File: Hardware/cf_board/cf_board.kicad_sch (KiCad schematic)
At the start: 14 parts, among them J1 Conn_01x40, J2 Conn_02x25_Top_Bottom, U1 74HC00, U2 74HC00

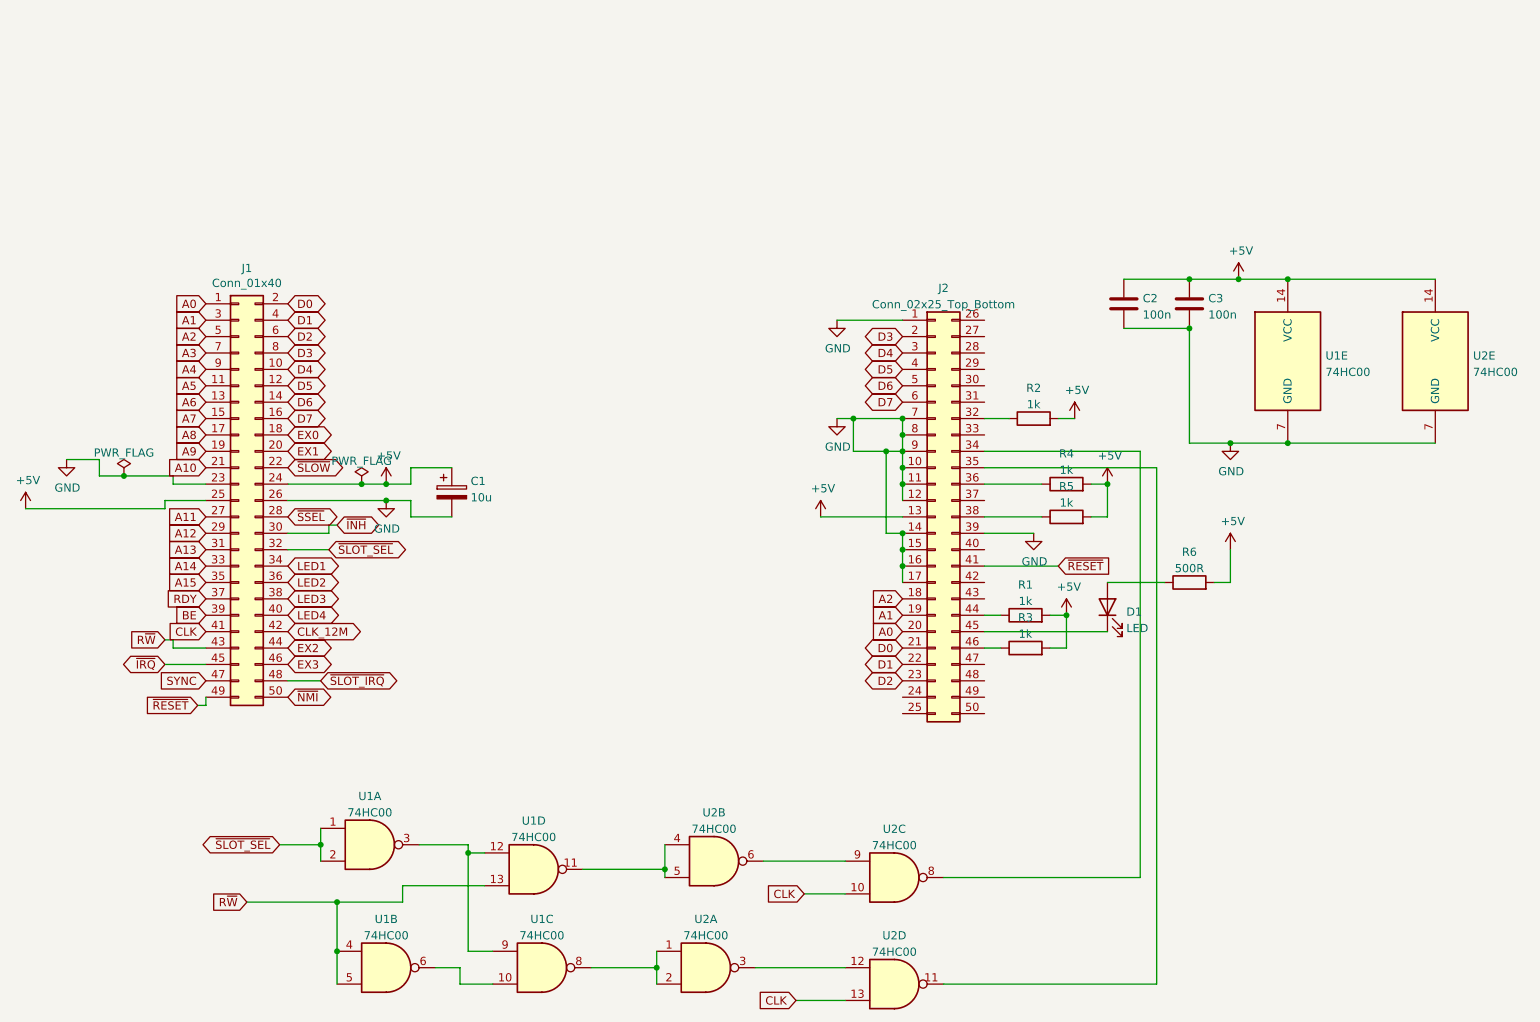
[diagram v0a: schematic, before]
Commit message: update with lcsc CF card socket
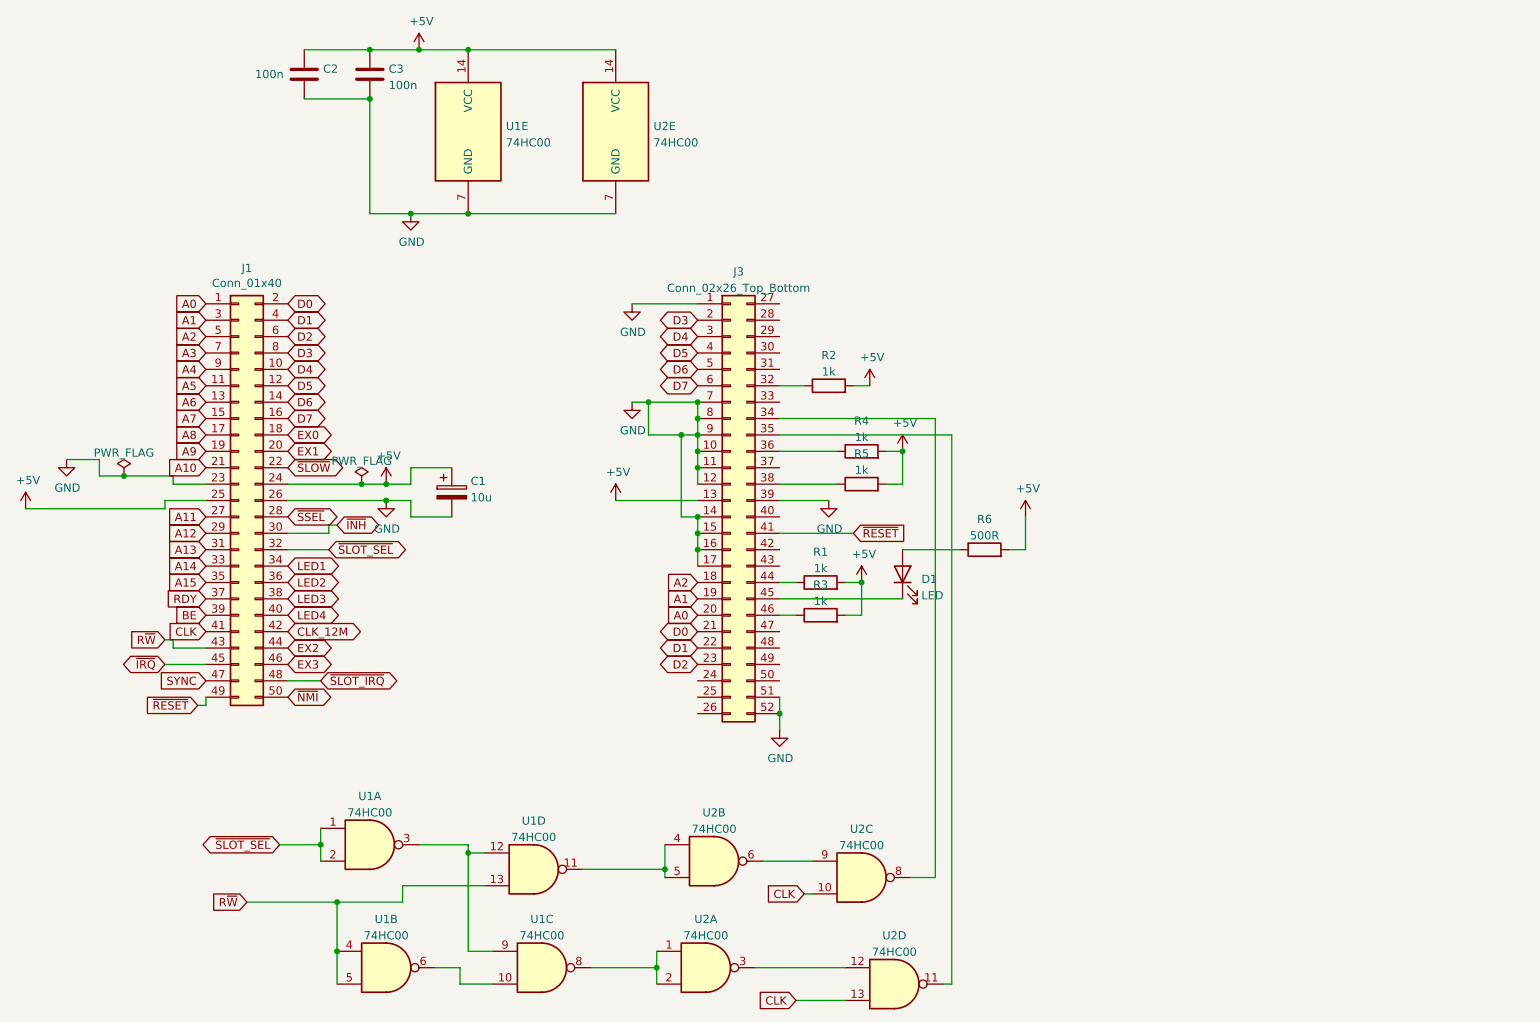
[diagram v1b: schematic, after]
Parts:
- removed J2: Conn_02x25_Top_Bottom, Connector_Card:CF-Card_3M_N7E50-A516xx-30, symbol Connector_Generic:Conn_02x25_Top_Bottom
- added J3: Conn_02x26_Top_Bottom, Custom_Footprints:SD-SMD_CFH-L3C1LBL01MN0, symbol Connector_Generic:Conn_02x26_Top_Bottom
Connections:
- net +5V: now also J3.13 (Pin_13)
- net A0: now also J3.20 (Pin_20)
- net A1: now also J3.19 (Pin_19)
- net A2: now also J3.18 (Pin_18)
- net D0: now also J3.21 (Pin_21)
- net D1: now also J3.22 (Pin_22)
- net D2: now also J3.23 (Pin_23)
- net D3: now also J3.2 (Pin_2)
- net D4: now also J3.3 (Pin_3)
- net D5: now also J3.4 (Pin_4)
- net D6: now also J3.5 (Pin_5)
- net D7: now also J3.6 (Pin_6)
- net GND: now also J3.1 (Pin_1), J3.10 (Pin_10), J3.11 (Pin_11), J3.12 (Pin_12), J3.14 (Pin_14), J3.15 (Pin_15), J3.16 (Pin_16), J3.17 (Pin_17), J3.39 (Pin_39), J3.51 (Pin_51), J3.52 (Pin_52), J3.7 (Pin_7), J3.8 (Pin_8), J3.9 (Pin_9)
- net ~{RESET}: now also J3.41 (Pin_41)
- net at R2.1: now also J3.32 (Pin_32)
- net at R3.1: now also J3.46 (Pin_46)
- net at U2.8: now also J3.34 (Pin_34)
- net at U2.11: now also J3.35 (Pin_35)
- net at D1.1 (K): now also J3.45 (Pin_45)
- net at R5.1: now also J3.38 (Pin_38)
- net at R4.1: now also J3.36 (Pin_36)
- net at R1.1: now also J3.44 (Pin_44)
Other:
- moved on the sheet: C2, C3, D1, R1, R2, R3, R4, R5, R6, U1E, U2C, U2E

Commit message: CF card works as block storage for forth
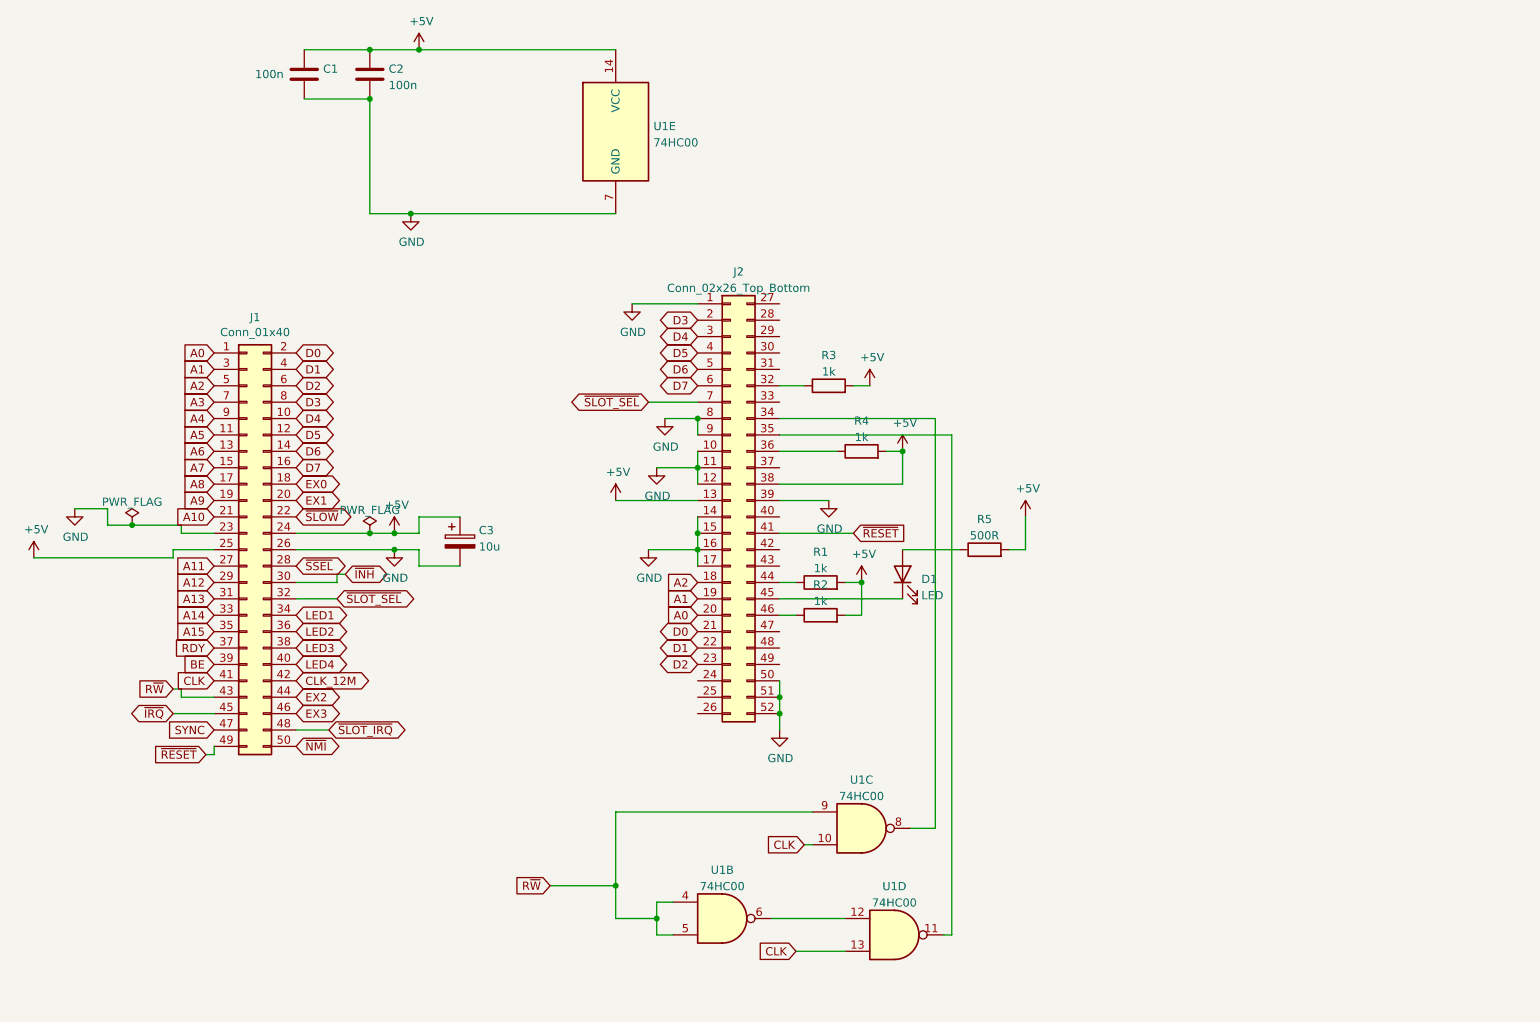
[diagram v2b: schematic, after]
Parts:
- removed R5: 1k, Resistor_THT:R_Axial_DIN0309_L9.0mm_D3.2mm_P12.70mm_Horizontal, symbol Device:R
- removed U1: 74HC00, Package_DIP:DIP-14_W7.62mm_Socket, symbol 74xx:74HC00
- removed unit 1 of U2
- renumbered C2 to C1, C3 to C2, C1 to C3, J3 to J2, R3 to R2, R2 to R3, R6 to R5, U2 to U1
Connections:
- net +5V: now also J2.38 (Pin_38)
- net GND: now also J2.50 (Pin_50); no longer J2.7 (Pin_7)
- net R~{W}: now also U1.4, U1.5, U1.9
- net ~{SLOT_SEL}: now also J2.7 (Pin_7)
- net at U1.6: now also U1.12; no longer U1.9
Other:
- moved on the sheet: C3, J1, U1B, U1C, U1D

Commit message: Add clock stretching + Simplify decoding.
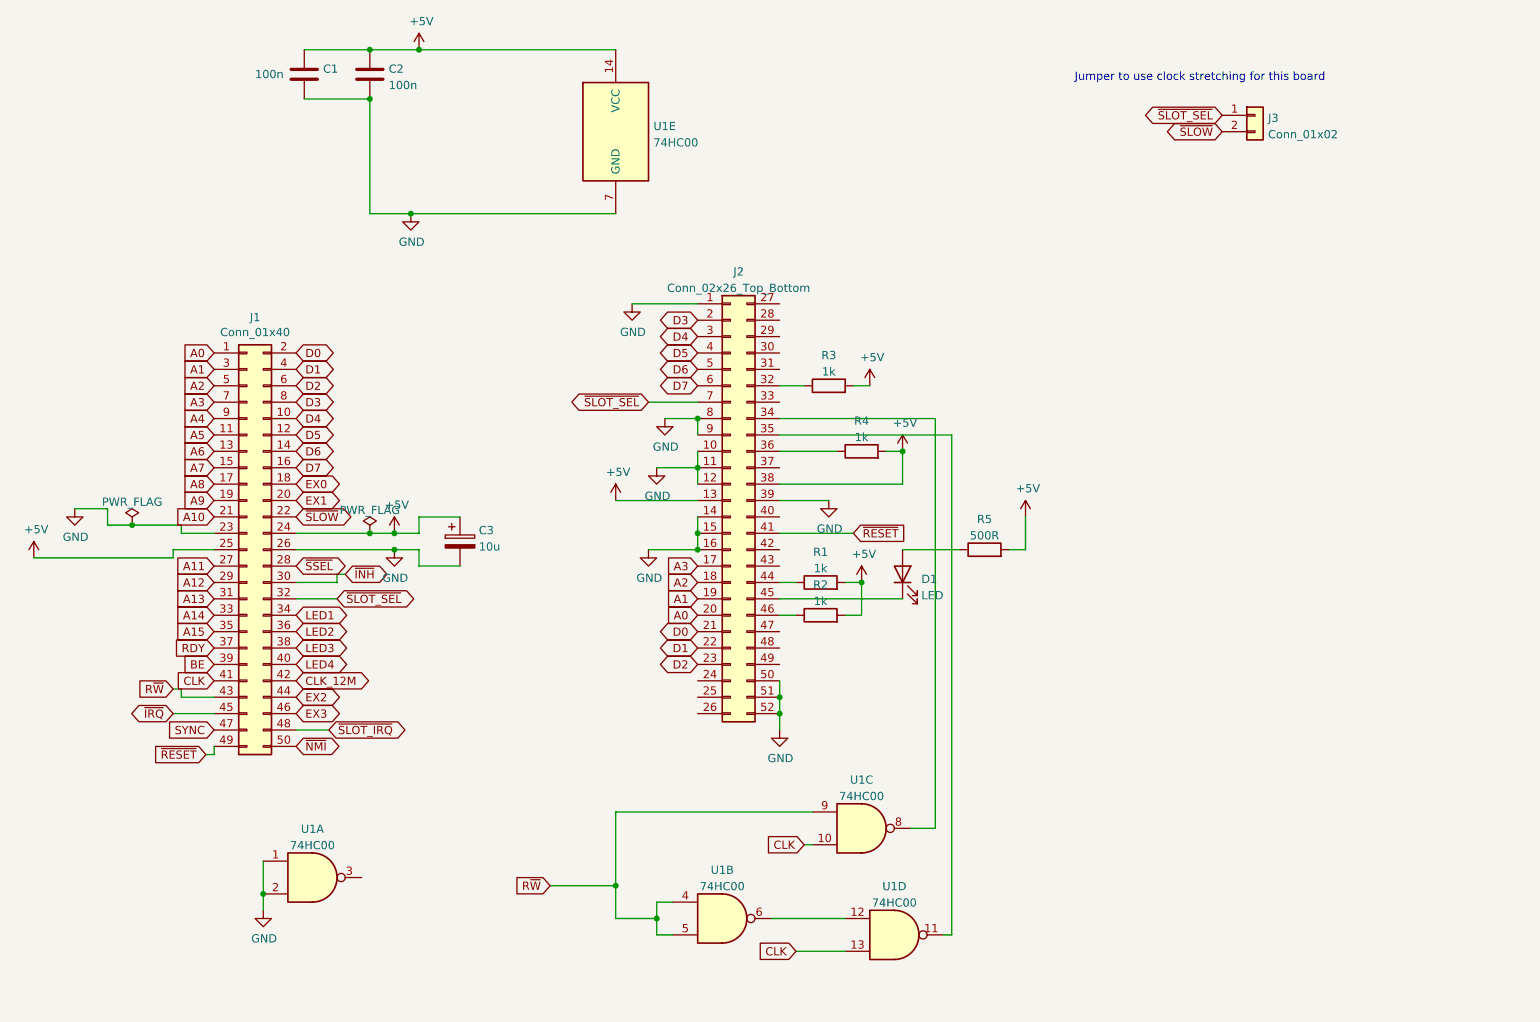
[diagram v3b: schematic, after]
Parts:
- added J3: Conn_01x02, Connector_PinHeader_2.54mm:PinHeader_1x02_P2.54mm_Vertical, symbol Connector_Generic:Conn_01x02
- added unit 1 of U1
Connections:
- net A3: now also J2.17 (Pin_17)
- net GND: now also U1.1, U1.2; no longer J2.17 (Pin_17)
- net ~{SLOT_SEL}: now also J3.1 (Pin_1)
- net ~{SLOW}: now also J3.2 (Pin_2)
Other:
- note added: "Jumper to use clock stretching for this board"

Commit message: Smaller resistors for CF card.
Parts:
- R1, R2, R3, R4, R5: footprint Resistor_THT:R_Axial_DIN0309_L9.0mm_D3.2mm_P12.70mm_Horizontal -> Resistor_THT:R_Axial_DIN0207_L6.3mm_D2.5mm_P10.16mm_Horizontal
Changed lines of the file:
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@@
     (property "Reference" "R3" (id 0) (at 146.05 67.6742 90))
     (property "Value" "1k" (id 1) (at 146.05 70.2111 90))
-    (property "Footprint" "Resistor_THT:R_Axial_DIN0309_L9.0mm_D3.2mm_P12.70mm_Horizontal" (id 2) (at 146.05 74.168 90)
+    (property "Footprint" "Resistor_THT:R_Axial_DIN0207_L6.3mm_D2.5mm_P10.16mm_Horizontal" (id 2) (at 146.05 74.168 90)
       (effects (font (size 1.27 1.27)) hide)
     )
@@
     (property "Reference" "R2" (id 0) (at 144.78 103.2342 90))
     (property "Value" "1k" (id 1) (at 144.78 105.7711 90))
-    (property "Footprint" "Resistor_THT:R_Axial_DIN0309_L9.0mm_D3.2mm_P12.70mm_Horizontal" (id 2) (at 144.78 109.728 90)
+    (property "Footprint" "Resistor_THT:R_Axial_DIN0207_L6.3mm_D2.5mm_P10.16mm_Horizontal" (id 2) (at 144.78 109.728 90)
       (effects (font (size 1.27 1.27)) hide)
     )
@@
     (property "Reference" "R1" (id 0) (at 144.78 98.1542 90))
     (property "Value" "1k" (id 1) (at 144.78 100.6911 90))
-    (property "Footprint" "Resistor_THT:R_Axial_DIN0309_L9.0mm_D3.2mm_P12.70mm_Horizontal" (id 2) (at 144.78 104.648 90)
+    (property "Footprint" "Resistor_THT:R_Axial_DIN0207_L6.3mm_D2.5mm_P10.16mm_Horizontal" (id 2) (at 144.78 104.648 90)
       (effects (font (size 1.27 1.27)) hide)
     )
@@
     (property "Reference" "R4" (id 0) (at 151.13 77.8342 90))
     (property "Value" "1k" (id 1) (at 151.13 80.3711 90))
-    (property "Footprint" "Resistor_THT:R_Axial_DIN0309_L9.0mm_D3.2mm_P12.70mm_Horizontal" (id 2) (at 151.13 84.328 90)
+    (property "Footprint" "Resistor_THT:R_Axial_DIN0207_L6.3mm_D2.5mm_P10.16mm_Horizontal" (id 2) (at 151.13 84.328 90)
       (effects (font (size 1.27 1.27)) hide)
     )
@@
     (property "Reference" "R5" (id 0) (at 170.18 93.0742 90))
     (property "Value" "500R" (id 1) (at 170.18 95.6111 90))
-    (property "Footprint" "Resistor_THT:R_Axial_DIN0309_L9.0mm_D3.2mm_P12.70mm_Horizontal" (id 2) (at 170.18 99.568 90)
+    (property "Footprint" "Resistor_THT:R_Axial_DIN0207_L6.3mm_D2.5mm_P10.16mm_Horizontal" (id 2) (at 170.18 99.568 90)
       (effects (font (size 1.27 1.27)) hide)
     )
@@
     )
     (path "/d941e788-4b41-41c3-af8e-4a1584f48b26"
-      (reference "R1") (unit 1) (value "1k") (footprint "Resistor_THT:R_Axial_DIN0309_L9.0mm_D3.2mm_P12.70mm_Horizontal")
+      (reference "R1") (unit 1) (value "1k") (footprint "Resistor_THT:R_Axial_DIN0207_L6.3mm_D2.5mm_P10.16mm_Horizontal")
     )
     (path "/4016a720-4a5b-43e6-8b57-97fcc9db399b"
-      (reference "R2") (unit 1) (value "1k") (footprint "Resistor_THT:R_Axial_DIN0309_L9.0mm_D3.2mm_P12.70mm_Horizontal")
+      (reference "R2") (unit 1) (value "1k") (footprint "Resistor_THT:R_Axial_DIN0207_L6.3mm_D2.5mm_P10.16mm_Horizontal")
     )
     (path "/13d409ad-2aeb-4c42-9a49-cbe2c4c32a40"
-      (reference "R3") (unit 1) (value "1k") (footprint "Resistor_THT:R_Axial_DIN0309_L9.0mm_D3.2mm_P12.70mm_Horizontal")
+      (reference "R3") (unit 1) (value "1k") (footprint "Resistor_THT:R_Axial_DIN0207_L6.3mm_D2.5mm_P10.16mm_Horizontal")
     )
     (path "/f2a75975-f2d1-4ddd-8906-70091a37ead6"
-      (reference "R4") (unit 1) (value "1k") (footprint "Resistor_THT:R_Axial_DIN0309_L9.0mm_D3.2mm_P12.70mm_Horizontal")
+      (reference "R4") (unit 1) (value "1k") (footprint "Resistor_THT:R_Axial_DIN0207_L6.3mm_D2.5mm_P10.16mm_Horizontal")
     )
     (path "/f50ba3ee-8c27-4175-9de1-0c6962b87c01"
-      (reference "R5") (unit 1) (value "500R") (footprint "Resistor_THT:R_Axial_DIN0309_L9.0mm_D3.2mm_P12.70mm_Horizontal")
+      (reference "R5") (unit 1) (value "500R") (footprint "Resistor_THT:R_Axial_DIN0207_L6.3mm_D2.5mm_P10.16mm_Horizontal")
     )
     (path "/a93c04ed-0f3d-4a98-8859-2aec35416613"
